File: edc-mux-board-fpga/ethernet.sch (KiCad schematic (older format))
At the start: 38 parts, among them U57 W5500

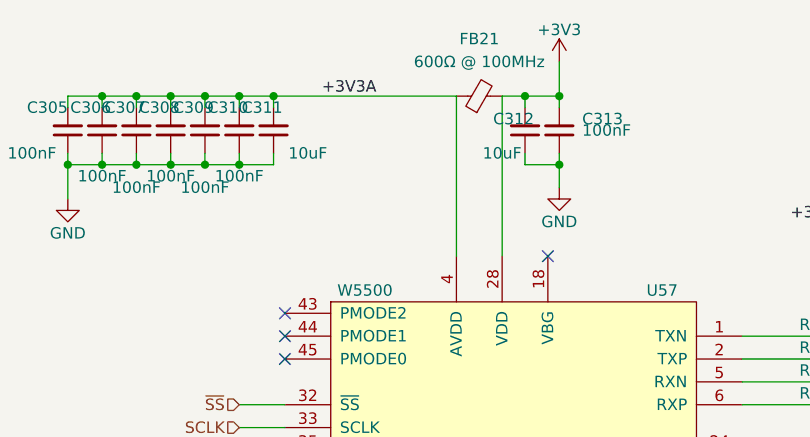
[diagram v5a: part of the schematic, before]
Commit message: assigned more footprints
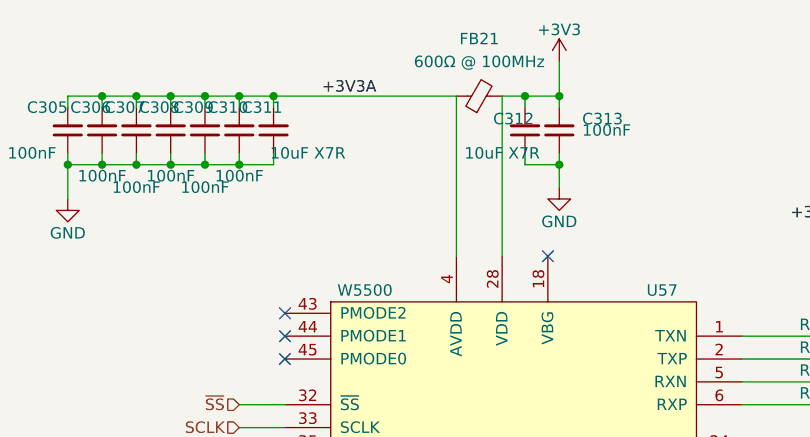
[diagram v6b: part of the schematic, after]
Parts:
- C305, C306, C307, C308, C309, C310, C313, C316, C317, C318, C319: footprint (none) -> Capacitor_SMD:C_0603_1608Metric; Package ID (none) -> 0603in/1608mm
- C311, C312: value 10uF -> 10uF X7R; footprint (none) -> Capacitor_SMD:C_1206_3216Metric; Manufacturer (none) -> Kemet; Manufacturers Part Number (none) -> C1206C106J3RACAUTO; Package ID (none) -> 1206in/3216mm
- C314, C315: footprint (none) -> Capacitor_SMD:C_0805_2012Metric; Package ID (none) -> 0805in/2012mm
- R103, R104, R105, R106, R107, R108, R109, R110, R111, R112, R113, R114, R115, R116, R117, R118, R119, R120, R121, R122: footprint (none) -> Resistor_SMD:R_0402_1005Metric
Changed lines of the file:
@@
 $Descr A4 11693 8268
 encoding utf-8
-Sheet 24 28
+Sheet 23 28
 Title ""
 Date ""
@@
 F 0 "R106" V 7350 2600 50  0000 L CNN
 F 1 "0Ω" V 7350 2800 50  0000 L CNN
-F 2 "" H 7400 2750 50  0001 C CNN
+F 2 "Resistor_SMD:R_0402_1005Metric" H 7400 2750 50  0001 C CNN
 F 3 "~" H 7400 2750 50  0001 C CNN
 	1    7400 2750
@@
 F 0 "R107" V 7350 2700 50  0000 L CNN
 F 1 "0Ω" V 7350 2900 50  0000 L CNN
-F 2 "" H 7400 2850 50  0001 C CNN
+F 2 "Resistor_SMD:R_0402_1005Metric" H 7400 2850 50  0001 C CNN
 F 3 "~" H 7400 2850 50  0001 C CNN
 	1    7400 2850
@@
 F 0 "R108" V 7350 2800 50  0000 L CNN
 F 1 "0Ω" V 7350 3000 50  0000 L CNN
-F 2 "" H 7400 2950 50  0001 C CNN
+F 2 "Resistor_SMD:R_0402_1005Metric" H 7400 2950 50  0001 C CNN
 F 3 "~" H 7400 2950 50  0001 C CNN
 	1    7400 2950
@@
 F 0 "R110" V 7350 2900 50  0000 L CNN
 F 1 "0Ω" V 7350 3100 50  0000 L CNN
-F 2 "" H 7400 3050 50  0001 C CNN
+F 2 "Resistor_SMD:R_0402_1005Metric" H 7400 3050 50  0001 C CNN
 F 3 "~" H 7400 3050 50  0001 C CNN
 	1    7400 3050
@@
 F 0 "R103" H 7730 2570 50  0000 L CNN
 F 1 "49.9Ω 1%" V 7750 2100 50  0000 L CNN
-F 2 "" H 7700 2550 50  0001 C CNN
+F 2 "Resistor_SMD:R_0402_1005Metric" H 7700 2550 50  0001 C CNN
 F 3 "~" H 7700 2550 50  0001 C CNN
 	1    7700 2550
@@
 F 0 "R104" H 7930 2570 50  0000 L CNN
 F 1 "49.9Ω 1%" V 7950 2100 50  0000 L CNN
-F 2 "" H 7900 2550 50  0001 C CNN
+F 2 "Resistor_SMD:R_0402_1005Metric" H 7900 2550 50  0001 C CNN
 F 3 "~" H 7900 2550 50  0001 C CNN
 	1    7900 2550
@@
 F 0 "R105" H 7950 2500 50  0000 R CNN
 F 1 "10Ω 1%" H 7950 2550 50  0000 R CNN
-F 2 "" H 8050 2550 50  0001 C CNN
+F 2 "Resistor_SMD:R_0402_1005Metric" H 8050 2550 50  0001 C CNN
 F 3 "~" H 8050 2550 50  0001 C CNN
 	1    8050 2550
@@
 F 0 "C316" H 8060 3670 50  0000 L CNN
 F 1 "22nF" H 8060 3520 50  0000 L CNN
-F 2 "" H 8050 3600 50  0001 C CNN
+F 2 "Capacitor_SMD:C_0603_1608Metric" H 8050 3600 50  0001 C CNN
 F 3 "~" H 8050 3600 50  0001 C CNN
+F 4 "0603in/1608mm" H 0   0   50  0001 C CNN "Package ID"
 	1    8050 3600
 	1    0    0    -1
@@
 F 0 "R114" H 7700 3500 50  0000 L CNN
 F 1 "82Ω 1%" H 7400 3700 50  0000 L CNN
-F 2 "" H 7700 3600 50  0001 C CNN
+F 2 "Resistor_SMD:R_0402_1005Metric" H 7700 3600 50  0001 C CNN
 F 3 "~" H 7700 3600 50  0001 C CNN
 	1    7700 3600
@@
 F 0 "C314" V 7650 3200 50  0000 C CNN
 F 1 "6.8uF" V 7750 3200 50  0000 C CNN
-F 2 "" H 7900 3200 50  0001 C CNN
+F 2 "Capacitor_SMD:C_0805_2012Metric" H 7900 3200 50  0001 C CNN
 F 3 "~" H 7900 3200 50  0001 C CNN
+F 4 "0805in/2012mm" H 0   0   50  0001 C CNN "Package ID"
 	1    7900 3200
 	0    1    1    0
@@
 F 0 "C315" V 8100 3400 50  0000 C CNN
 F 1 "6.8uF" V 8000 3400 50  0000 C CNN
-F 2 "" H 7900 3400 50  0001 C CNN
+F 2 "Capacitor_SMD:C_0805_2012Metric" H 7900 3400 50  0001 C CNN
 F 3 "~" H 7900 3400 50  0001 C CNN
+F 4 "0805in/2012mm" H 0   0   50  0001 C CNN "Package ID"
 	1    7900 3400
 	0    1    1    0
@@
 F 0 "R113" H 7600 3500 50  0000 L CNN
 F 1 "82Ω 1%" H 7650 3700 50  0000 L CNN
-F 2 "" H 7600 3600 50  0001 C CNN
+F 2 "Resistor_SMD:R_0402_1005Metric" H 7600 3600 50  0001 C CNN
 F 3 "~" H 7600 3600 50  0001 C CNN
 	1    7600 3600
@@
 F 0 "R116" V 9300 4200 50  0000 R CNN
 F 1 "75Ω 1%" V 9400 4000 50  0000 R CNN
-F 2 "" H 9350 4050 50  0001 C CNN
+F 2 "Resistor_SMD:R_0402_1005Metric" H 9350 4050 50  0001 C CNN
 F 3 "~" H 9350 4050 50  0001 C CNN
 	1    9350 4050
@@
 F 0 "R117" V 9550 4200 50  0000 R CNN
 F 1 "75Ω 1%" V 9450 4000 50  0000 R CNN
-F 2 "" H 9500 4050 50  0001 C CNN
+F 2 "Resistor_SMD:R_0402_1005Metric" H 9500 4050 50  0001 C CNN
 F 3 "~" H 9500 4050 50  0001 C CNN
 	1    9500 4050
@@
 F 0 "C319" H 9410 4520 50  0000 L CNN
 F 1 "4.7nF" H 9410 4370 50  0000 L CNN
-F 2 "" H 9400 4450 50  0001 C CNN
+F 2 "Capacitor_SMD:C_0603_1608Metric" H 9400 4450 50  0001 C CNN
 F 3 "~" H 9400 4450 50  0001 C CNN
+F 4 "0603in/1608mm" H 0   0   50  0001 C CNN "Package ID"
 	1    9400 4450
 	1    0    0    -1
@@
 F 0 "R109" V 10450 3000 50  0000 C CNN
 F 1 "49.9Ω 1%" V 10350 3000 50  0000 C CNN
-F 2 "" H 10200 3000 50  0001 C CNN
+F 2 "Resistor_SMD:R_0402_1005Metric" H 10200 3000 50  0001 C CNN
 F 3 "~" H 10200 3000 50  0001 C CNN
 	1    10200 3000
@@
 F 0 "R120" V 9950 4200 50  0000 R CNN
 F 1 "49.9Ω 1%" V 9850 4000 50  0000 R CNN
-F 2 "" H 9900 4050 50  0001 C CNN
+F 2 "Resistor_SMD:R_0402_1005Metric" H 9900 4050 50  0001 C CNN
 F 3 "~" H 9900 4050 50  0001 C CNN
 	1    9900 4050
@@
 F 0 "R111" V 10350 3100 50  0000 C CNN
 F 1 "49.9Ω 1%" V 10300 3100 50  0000 C CNN
-F 2 "" H 10200 3100 50  0001 C CNN
+F 2 "Resistor_SMD:R_0402_1005Metric" H 10200 3100 50  0001 C CNN
 F 3 "~" H 10200 3100 50  0001 C CNN
 	1    10200 3100
@@
 F 0 "R112" V 10400 3550 50  0000 C CNN
 F 1 "49.9Ω 1%" V 10300 3550 50  0000 C CNN
-F 2 "" H 10200 3550 50  0001 C CNN
+F 2 "Resistor_SMD:R_0402_1005Metric" H 10200 3550 50  0001 C CNN
 F 3 "~" H 10200 3550 50  0001 C CNN
 	1    10200 3550
@@
 F 0 "R115" V 10400 3650 50  0000 C CNN
 F 1 "49.9Ω 1%" V 10300 3550 50  0000 C CNN
-F 2 "" H 10200 3650 50  0001 C CNN
+F 2 "Resistor_SMD:R_0402_1005Metric" H 10200 3650 50  0001 C CNN
 F 3 "~" H 10200 3650 50  0001 C CNN
 	1    10200 3650
@@
 F 0 "R121" V 10100 4200 50  0000 R CNN
 F 1 "49.9Ω 1%" H 10000 4150 50  0000 R CNN
-F 2 "" H 10050 4050 50  0001 C CNN
+F 2 "Resistor_SMD:R_0402_1005Metric" H 10050 4050 50  0001 C CNN
 F 3 "~" H 10050 4050 50  0001 C CNN
 	1    10050 4050
@@
 F 0 "R118" V 9700 4200 50  0000 R CNN
 F 1 "150Ω 1%" V 9600 4000 50  0000 R CNN
-F 2 "" H 9650 4050 50  0001 C CNN
+F 2 "Resistor_SMD:R_0402_1005Metric" H 9650 4050 50  0001 C CNN
 F 3 "~" H 9650 4050 50  0001 C CNN
 	1    9650 4050
@@
 F 0 "R119" V 9800 4200 50  0000 R CNN
 F 1 "150Ω 1%" V 9700 4000 50  0000 R CNN
-F 2 "" H 9750 4050 50  0001 C CNN
+F 2 "Resistor_SMD:R_0402_1005Metric" H 9750 4050 50  0001 C CNN
 F 3 "~" H 9750 4050 50  0001 C CNN
 	1    9750 4050
@@
 F 0 "C317" H 5960 4420 50  0000 L CNN
 F 1 "4.7nF" H 5960 4270 50  0000 L CNN
-F 2 "" H 5950 4350 50  0001 C CNN
+F 2 "Capacitor_SMD:C_0603_1608Metric" H 5950 4350 50  0001 C CNN
 F 3 "~" H 5950 4350 50  0001 C CNN
+F 4 "0603in/1608mm" H 0   0   50  0001 C CNN "Package ID"
 	1    5950 4350
 	1    0    0    -1
@@
 F 0 "C318" H 6410 4420 50  0000 L CNN
 F 1 "10nF" H 6410 4270 50  0000 L CNN
-F 2 "" H 6400 4350 50  0001 C CNN
+F 2 "Capacitor_SMD:C_0603_1608Metric" H 6400 4350 50  0001 C CNN
 F 3 "~" H 6400 4350 50  0001 C CNN
+F 4 "0603in/1608mm" H 0   0   50  0001 C CNN "Package ID"
 	1    6400 4350
 	1    0    0    -1
@@
 F 0 "C313" H 6100 1800 50  0000 R CNN
 F 1 "100nF" H 6100 1850 50  0000 R CNN
-F 2 "" H 6200 1850 50  0001 C CNN
+F 2 "Capacitor_SMD:C_0603_1608Metric" H 6200 1850 50  0001 C CNN
 F 3 "~" H 6200 1850 50  0001 C CNN
+F 4 "0603in/1608mm" H 0   0   50  0001 C CNN "Package ID"
 	1    6200 1850
 	-1   0    0    1
@@
 P 6050 1850
 F 0 "C312" H 6100 1800 50  0000 C CNN
-F 1 "10uF" H 6150 1950 50  0000 C CNN
-F 2 "" H 6050 1850 50  0001 C CNN
+F 1 "10uF X7R" H 6150 1950 50  0000 C CNN
+F 2 "Capacitor_SMD:C_1206_3216Metric" H 6050 1850 50  0001 C CNN
 F 3 "~" H 6050 1850 50  0001 C CNN
+F 4 "Kemet" H 0   0   50  0001 C CNN "Manufacturer"
+F 5 "C1206C106J3RACAUTO" H 0   0   50  0001 C CNN "Manufacturers Part Number"
+F 6 "1206in/3216mm" H 0   0   50  0001 C CNN "Package ID"
 	1    6050 1850
 	-1   0    0    1
@@
 F 0 "C310" H 4850 1750 50  0000 C CNN
 F 1 "100nF" H 4800 2050 50  0000 C CNN
-F 2 "" H 4800 1850 50  0001 C CNN
+F 2 "Capacitor_SMD:C_0603_1608Metric" H 4800 1850 50  0001 C CNN
 F 3 "~" H 4800 1850 50  0001 C CNN
+F 4 "0603in/1608mm" H 0   0   50  0001 C CNN "Package ID"
 	1    4800 1850
 	-1   0    0    1
@@
 P 4950 1850
 F 0 "C311" H 5000 1750 50  0000 C CNN
-F 1 "10uF" H 4800 1950 50  0000 C CNN
-F 2 "" H 4950 1850 50  0001 C CNN
+F 1 "10uF X7R" H 4800 1950 50  0000 C CNN
+F 2 "Capacitor_SMD:C_1206_3216Metric" H 4950 1850 50  0001 C CNN
 F 3 "~" H 4950 1850 50  0001 C CNN
+F 4 "Kemet" H 0   0   50  0001 C CNN "Manufacturer"
+F 5 "C1206C106J3RACAUTO" H 0   0   50  0001 C CNN "Manufacturers Part Number"
+F 6 "1206in/3216mm" H 0   0   50  0001 C CNN "Package ID"
 	1    4950 1850
 	-1   0    0    1
@@
 F 0 "C309" H 4700 1750 50  0000 C CNN
 F 1 "100nF" H 4650 2100 50  0000 C CNN
-F 2 "" H 4650 1850 50  0001 C CNN
+F 2 "Capacitor_SMD:C_0603_1608Metric" H 4650 1850 50  0001 C CNN
 F 3 "~" H 4650 1850 50  0001 C CNN
+F 4 "0603in/1608mm" H 0   0   50  0001 C CNN "Package ID"
 	1    4650 1850
 	-1   0    0    1
@@
 F 0 "C308" H 4550 1750 50  0000 C CNN
 F 1 "100nF" H 4500 2050 50  0000 C CNN
-F 2 "" H 4500 1850 50  0001 C CNN
+F 2 "Capacitor_SMD:C_0603_1608Metric" H 4500 1850 50  0001 C CNN
 F 3 "~" H 4500 1850 50  0001 C CNN
+F 4 "0603in/1608mm" H 0   0   50  0001 C CNN "Package ID"
 	1    4500 1850
 	-1   0    0    1
@@
 F 0 "C307" H 4400 1750 50  0000 C CNN
 F 1 "100nF" H 4350 2100 50  0000 C CNN
-F 2 "" H 4350 1850 50  0001 C CNN
+F 2 "Capacitor_SMD:C_0603_1608Metric" H 4350 1850 50  0001 C CNN
 F 3 "~" H 4350 1850 50  0001 C CNN
+F 4 "0603in/1608mm" H 0   0   50  0001 C CNN "Package ID"
 	1    4350 1850
 	-1   0    0    1
@@
 F 0 "C306" H 4250 1750 50  0000 C CNN
 F 1 "100nF" H 4200 2050 50  0000 C CNN
-F 2 "" H 4200 1850 50  0001 C CNN
+F 2 "Capacitor_SMD:C_0603_1608Metric" H 4200 1850 50  0001 C CNN
 F 3 "~" H 4200 1850 50  0001 C CNN
+F 4 "0603in/1608mm" H 0   0   50  0001 C CNN "Package ID"
 	1    4200 1850
 	-1   0    0    1
@@
 F 0 "C305" H 4050 1750 50  0000 L CNN
 F 1 "100nF" H 4100 1950 50  0000 L CNN
-F 2 "" H 4050 1850 50  0001 C CNN
+F 2 "Capacitor_SMD:C_0603_1608Metric" H 4050 1850 50  0001 C CNN
 F 3 "~" H 4050 1850 50  0001 C CNN
+F 4 "0603in/1608mm" H 0   0   50  0001 C CNN "Package ID"
 	1    4050 1850
 	-1   0    0    1
@@
 F 0 "R122" H 7100 4250 50  0000 L CNN
 F 1 "12k4Ω 1%" H 7150 4450 50  0000 L CNN
-F 2 "" H 7100 4350 50  0001 C CNN
+F 2 "Resistor_SMD:R_0402_1005Metric" H 7100 4350 50  0001 C CNN
 F 3 "~" H 7100 4350 50  0001 C CNN
 	1    7100 4350

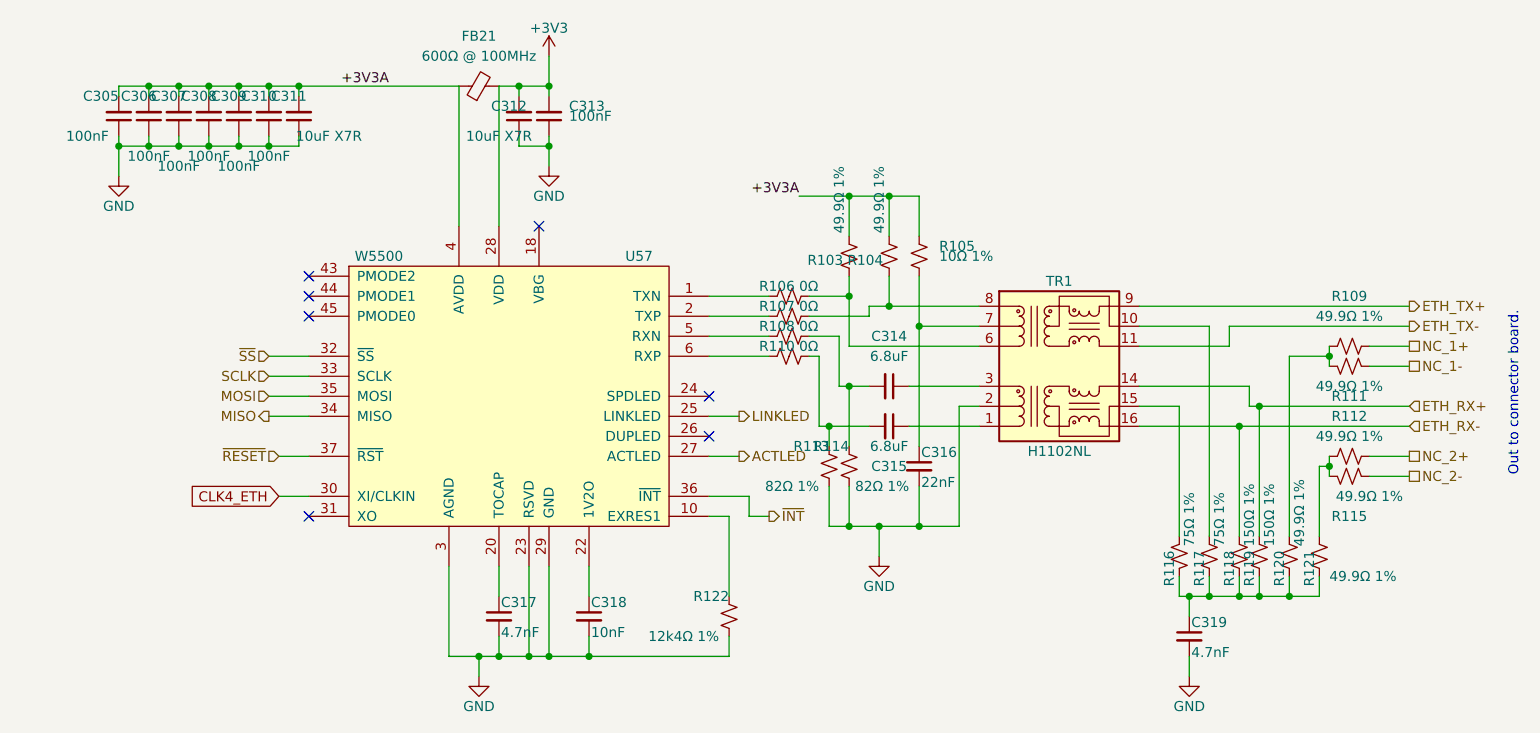
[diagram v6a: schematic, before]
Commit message: re-annotating after adding power ICs and decoupling capacitors.
Also verified most footprints, and updated schematic field data.
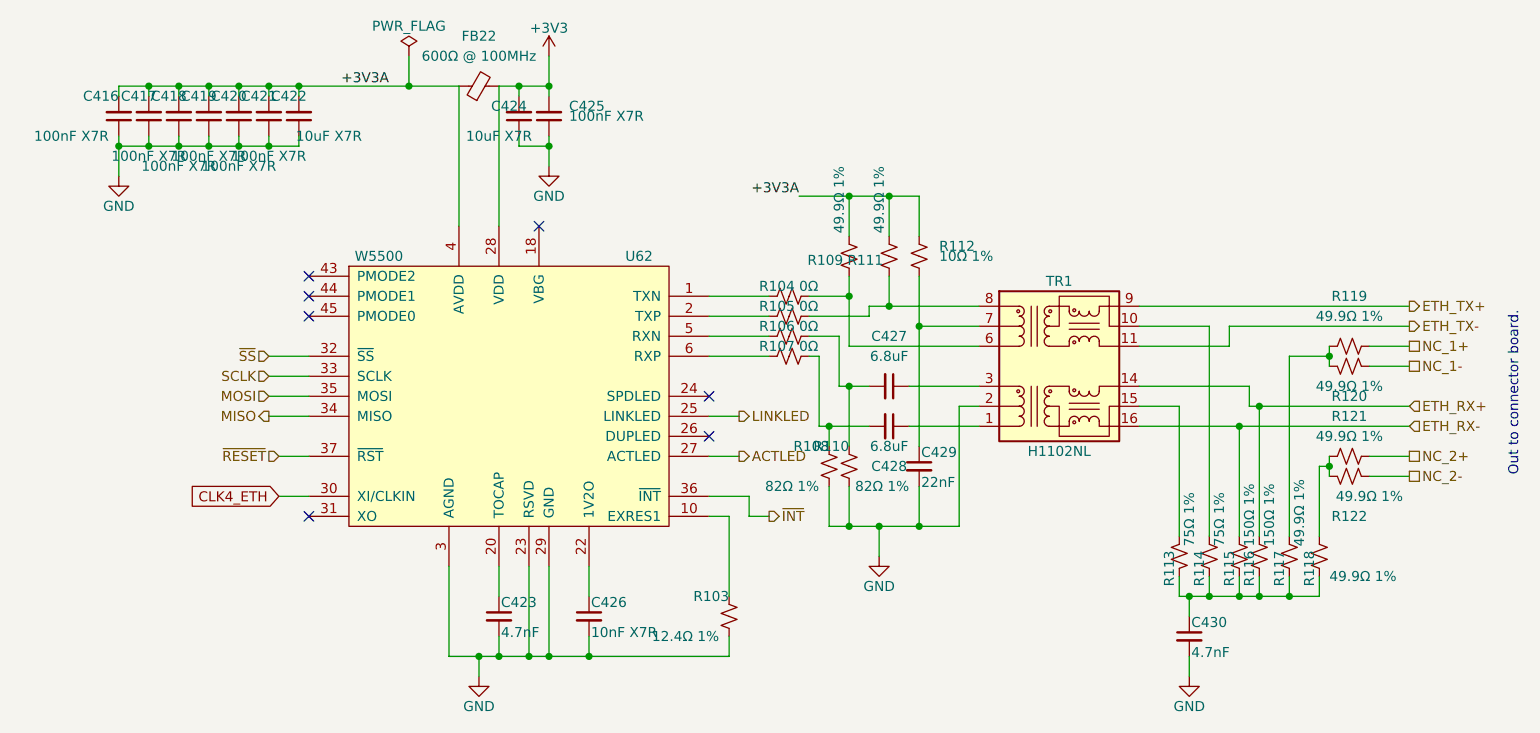
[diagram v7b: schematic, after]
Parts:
- C416: renamed from C305; value 100nF -> 100nF X7R
- C417: renamed from C306; value 100nF -> 100nF X7R
- C418: renamed from C307; value 100nF -> 100nF X7R
- C419: renamed from C308; value 100nF -> 100nF X7R
- C420: renamed from C309; value 100nF -> 100nF X7R
- C421: renamed from C310; value 100nF -> 100nF X7R
- C425: renamed from C313; value 100nF -> 100nF X7R
- C426: renamed from C318; value 10nF -> 10nF X7R; footprint Capacitor_SMD:C_0603_1608Metric -> Capacitor_SMD:C_0402_1005Metric; Package ID 0603in/1608mm -> 0402in/1005mm
- R103: renamed from R122; value 12k4Ω 1% -> 12.4Ω 1%; Package ID (none) -> 0402in/1005mm
- R104: renamed from R106; Package ID (none) -> 0402in/1005mm
- R105: renamed from R107; Package ID (none) -> 0402in/1005mm
- R106: renamed from R108; Package ID (none) -> 0402in/1005mm
- R107: renamed from R110; Package ID (none) -> 0402in/1005mm
- R108: renamed from R113; Package ID (none) -> 0402in/1005mm
- R109: renamed from R103; Package ID (none) -> 0402in/1005mm
- R110: renamed from R114; Package ID (none) -> 0402in/1005mm
- R111: renamed from R104; Package ID (none) -> 0402in/1005mm
- R112: renamed from R105; Package ID (none) -> 0402in/1005mm
- R113: renamed from R116; Package ID (none) -> 0402in/1005mm
- R114: renamed from R117; Package ID (none) -> 0402in/1005mm
- R115: renamed from R118; Package ID (none) -> 0402in/1005mm
- R116: renamed from R119; Package ID (none) -> 0402in/1005mm
- R117: renamed from R120; Package ID (none) -> 0402in/1005mm
- R118: renamed from R121; Package ID (none) -> 0402in/1005mm
- R119: renamed from R109; Package ID (none) -> 0402in/1005mm
- R120: renamed from R111; Package ID (none) -> 0402in/1005mm
- R121: renamed from R112; Package ID (none) -> 0402in/1005mm
- R122: renamed from R115; Package ID (none) -> 0402in/1005mm
- renumbered C311 to C422, C317 to C423, C312 to C424, C314 to C427, C315 to C428, C316 to C429, C319 to C430, FB21 to FB22, U57 to U62
